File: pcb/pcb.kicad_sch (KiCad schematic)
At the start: 15 parts

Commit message: Shift to 2.2k resistors and 2V LEDs for brightness
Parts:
- R1, R2: LCSC C17539 -> C17533; MPN RSF100JB-73-6K8 -> MFR01SF2201A10
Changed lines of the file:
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@@
 			(effects (font (size 1.27 1.27)) hide)
 		)
-		(property "MPN" "RSF100JB-73-6K8" (at 114.3 50.8 0)
+		(property "MPN" "MFR01SF2201A10" (at 114.3 50.8 0)
 			(effects (font (size 1.27 1.27)) hide)
 		)
-		(property "LCSC" "C17539" (at 114.3 50.8 0)
+		(property "LCSC" "C17533" (at 114.3 50.8 0)
 			(effects (font (size 1.27 1.27)) hide)
 		)
@@
 			(effects (font (size 1.27 1.27)) hide)
 		)
-		(property "MPN" "RSF100JB-73-6K8" (at 114.3 88.9 0)
+		(property "MPN" "MFR01SF2201A10" (at 114.3 88.9 0)
 			(effects (font (size 1.27 1.27)) hide)
 		)
-		(property "LCSC" "C17539" (at 114.3 88.9 0)
+		(property "LCSC" "C17533" (at 114.3 88.9 0)
 			(effects (font (size 1.27 1.27)) hide)
 		)

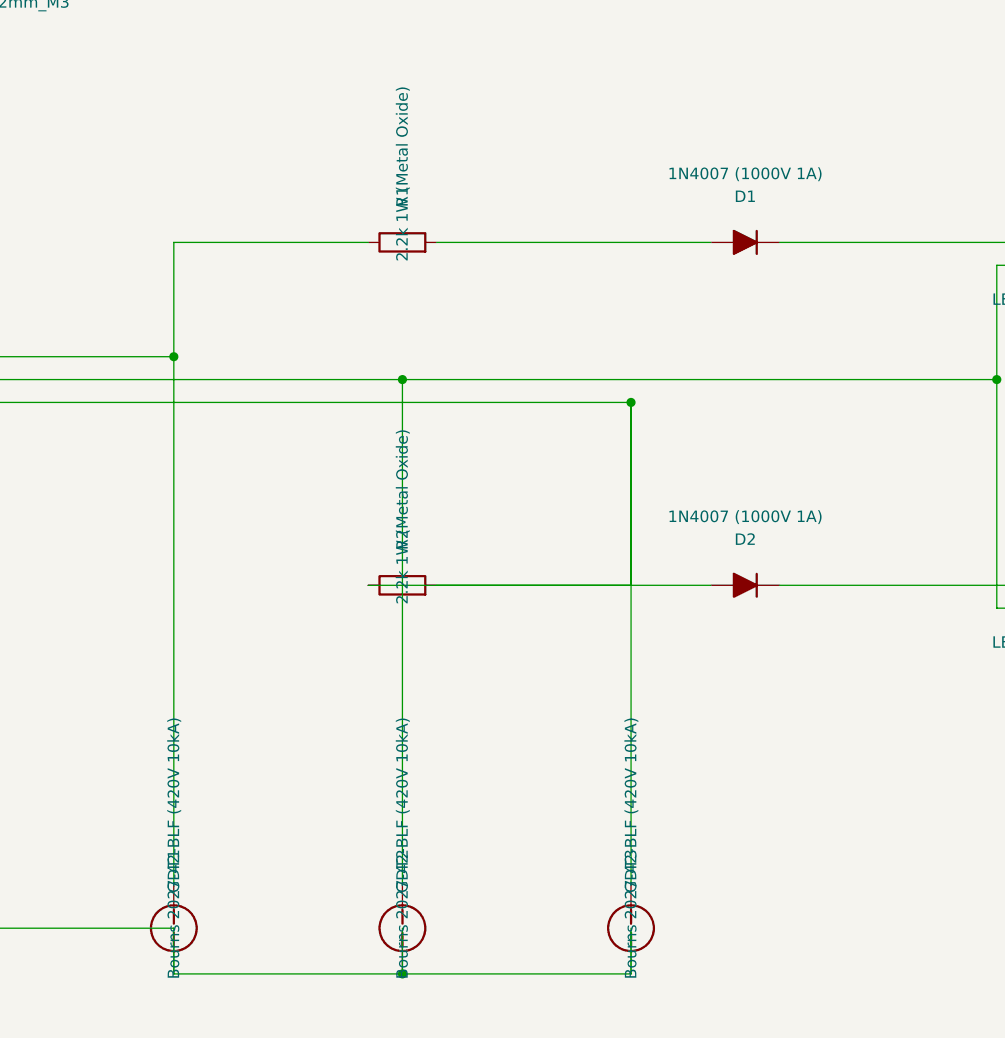
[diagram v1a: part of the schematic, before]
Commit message: Clean up pcb/ generated files in favour of Makefile and build/ dir
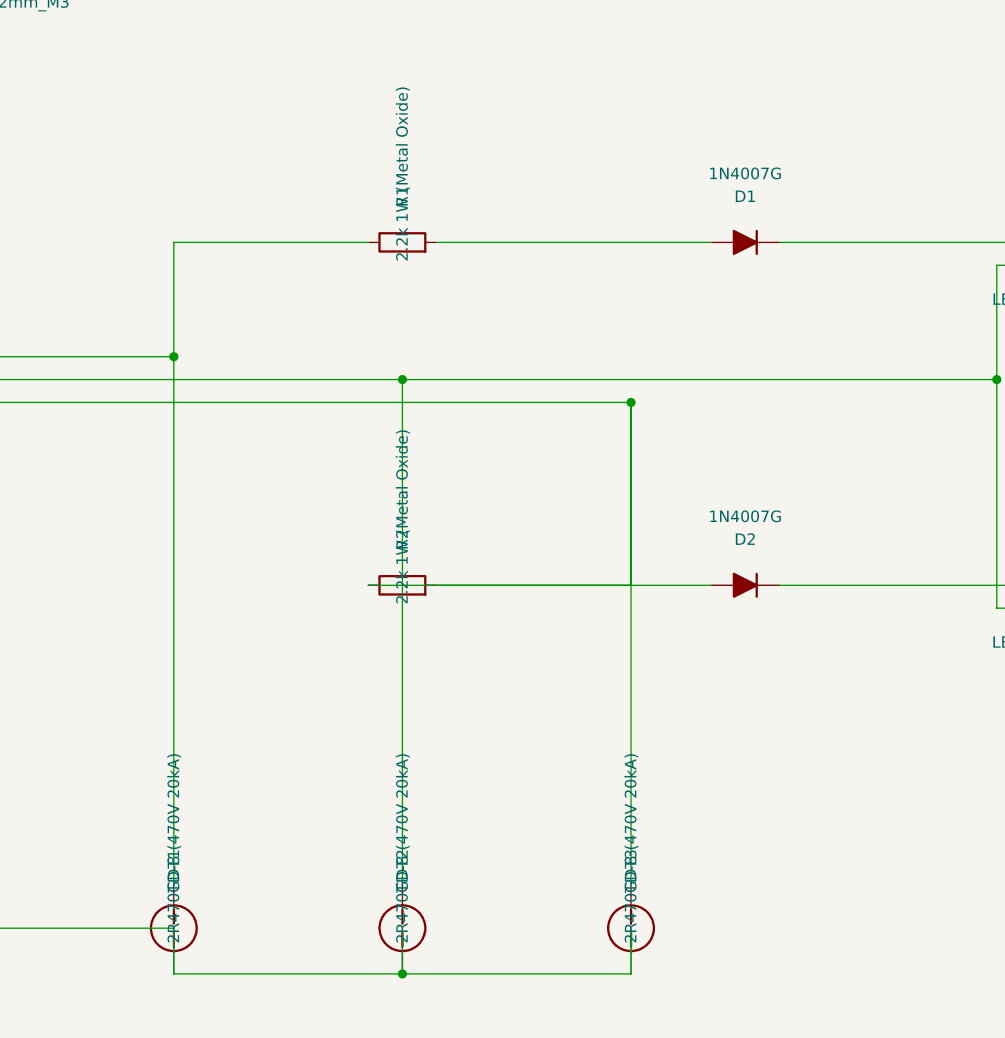
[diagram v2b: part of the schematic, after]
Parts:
- D1, D2: value 1N4007 (1000V 1A) -> 1N4007G; LCSC C2837 -> C232439; MPN 1N4007-E3/54 -> 1N4007G
- GDT1, GDT2, GDT3: value Bourns 2027-42-BLF (420V 10kA) -> 2R470TD-8 (470V 20kA); LCSC C2837330 -> C2836978; MPN 2027-42-BLF -> 2R470TD-8
- J_EARTH, J_LED_A, J_LED_C: LCSC C8464 -> C475092; MPN MKDS 1,5/ 2-5,08 -> KF129-5.08-2P
- J_IN: LCSC C8465 -> C474953; MPN MKDS 1,5/ 3-5,08 -> KF128-5.08-3P
- R1, R2: LCSC C17533 -> ASSIGN_BY_JLCPCB
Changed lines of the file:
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@@
 			(effects (font (size 1.27 1.27)) hide)
 		)
-		(property "MPN" "MKDS 1,5/ 3-5,08" (at 38.1 63.5 0)
-			(effects (font (size 1.27 1.27)) hide)
-		)
-		(property "LCSC" "C8465" (at 38.1 63.5 0)
+		(property "MPN" "KF128-5.08-3P" (at 38.1 63.5 0)
+			(effects (font (size 1.27 1.27)) hide)
+		)
+		(property "LCSC" "C474953" (at 38.1 63.5 0)
 			(effects (font (size 1.27 1.27)) hide)
 		)
@@
 			(effects (font (size 1.27 1.27)) hide)
 		)
-		(property "MPN" "MKDS 1,5/ 2-5,08" (at 38.1 127 0)
-			(effects (font (size 1.27 1.27)) hide)
-		)
-		(property "LCSC" "C8464" (at 38.1 127 0)
+		(property "MPN" "KF129-5.08-2P" (at 38.1 127 0)
+			(effects (font (size 1.27 1.27)) hide)
+		)
+		(property "LCSC" "C475092" (at 38.1 127 0)
 			(effects (font (size 1.27 1.27)) hide)
 		)
@@
 			(effects (font (size 1.27 1.27)) hide)
 		)
-		(property "MPN" "MKDS 1,5/ 2-5,08" (at 190.5 50.8 0)
-			(effects (font (size 1.27 1.27)) hide)
-		)
-		(property "LCSC" "C8464" (at 190.5 50.8 0)
+		(property "MPN" "KF129-5.08-2P" (at 190.5 50.8 0)
+			(effects (font (size 1.27 1.27)) hide)
+		)
+		(property "LCSC" "C475092" (at 190.5 50.8 0)
 			(effects (font (size 1.27 1.27)) hide)
 		)
@@
 			(effects (font (size 1.27 1.27)) hide)
 		)
-		(property "MPN" "MKDS 1,5/ 2-5,08" (at 190.5 88.9 0)
-			(effects (font (size 1.27 1.27)) hide)
-		)
-		(property "LCSC" "C8464" (at 190.5 88.9 0)
+		(property "MPN" "KF129-5.08-2P" (at 190.5 88.9 0)
+			(effects (font (size 1.27 1.27)) hide)
+		)
+		(property "LCSC" "C475092" (at 190.5 88.9 0)
 			(effects (font (size 1.27 1.27)) hide)
 		)
@@
 			(effects (font (size 1.27 1.27)) hide)
 		)
-		(property "LCSC" "C17533" (at 114.3 50.8 0)
+		(property "LCSC" "ASSIGN_BY_JLCPCB" (at 114.3 50.8 0)
 			(effects (font (size 1.27 1.27)) hide)
 		)
@@
 			(effects (font (size 1.27 1.27)))
 		)
-		(property "Value" "1N4007 (1000V 1A)" (at 152.4 43.18 0)
+		(property "Value" "1N4007G" (at 152.4 43.18 0)
 			(effects (font (size 1.27 1.27)))
 		)
@@
 			(effects (font (size 1.27 1.27)) hide)
 		)
-		(property "MPN" "1N4007-E3/54" (at 152.4 50.8 0)
-			(effects (font (size 1.27 1.27)) hide)
-		)
-		(property "LCSC" "C2837" (at 152.4 50.8 0)
+		(property "MPN" "1N4007G" (at 152.4 50.8 0)
+			(effects (font (size 1.27 1.27)) hide)
+		)
+		(property "LCSC" "C232439" (at 152.4 50.8 0)
 			(effects (font (size 1.27 1.27)) hide)
 		)
@@
 			(effects (font (size 1.27 1.27)) hide)
 		)
-		(property "LCSC" "C17533" (at 114.3 88.9 0)
+		(property "LCSC" "ASSIGN_BY_JLCPCB" (at 114.3 88.9 0)
 			(effects (font (size 1.27 1.27)) hide)
 		)
@@
 			(effects (font (size 1.27 1.27)))
 		)
-		(property "Value" "1N4007 (1000V 1A)" (at 152.4 81.28 0)
+		(property "Value" "1N4007G" (at 152.4 81.28 0)
 			(effects (font (size 1.27 1.27)))
 		)
@@
 			(effects (font (size 1.27 1.27)) hide)
 		)
-		(property "MPN" "1N4007-E3/54" (at 152.4 88.9 0)
-			(effects (font (size 1.27 1.27)) hide)
-		)
-		(property "LCSC" "C2837" (at 152.4 88.9 0)
+		(property "MPN" "1N4007G" (at 152.4 88.9 0)
+			(effects (font (size 1.27 1.27)) hide)
+		)
+		(property "LCSC" "C232439" (at 152.4 88.9 0)
 			(effects (font (size 1.27 1.27)) hide)
 		)
@@
 			(effects (font (size 1.27 1.27)))
 		)
-		(property "Value" "Bourns 2027-42-BLF (420V 10kA)" (at 88.9 118.11 0)
+		(property "Value" "2R470TD-8 (470V 20kA)" (at 88.9 118.11 0)
 			(effects (font (size 1.27 1.27)))
 		)
@@
 			(effects (font (size 1.27 1.27)) hide)
 		)
-		(property "MPN" "2027-42-BLF" (at 88.9 127 0)
-			(effects (font (size 1.27 1.27)) hide)
-		)
-		(property "LCSC" "C2837330" (at 88.9 127 0)
+		(property "MPN" "2R470TD-8" (at 88.9 127 0)
+			(effects (font (size 1.27 1.27)) hide)
+		)
+		(property "LCSC" "C2836978" (at 88.9 127 0)
 			(effects (font (size 1.27 1.27)) hide)
 		)
@@
 			(effects (font (size 1.27 1.27)))
 		)
-		(property "Value" "Bourns 2027-42-BLF (420V 10kA)" (at 114.3 118.11 0)
+		(property "Value" "2R470TD-8 (470V 20kA)" (at 114.3 118.11 0)
 			(effects (font (size 1.27 1.27)))
 		)
@@
 			(effects (font (size 1.27 1.27)) hide)
 		)
-		(property "MPN" "2027-42-BLF" (at 114.3 127 0)
-			(effects (font (size 1.27 1.27)) hide)
-		)
-		(property "LCSC" "C2837330" (at 114.3 127 0)
+		(property "MPN" "2R470TD-8" (at 114.3 127 0)
+			(effects (font (size 1.27 1.27)) hide)
+		)
+		(property "LCSC" "C2836978" (at 114.3 127 0)
 			(effects (font (size 1.27 1.27)) hide)
 		)
@@
 			(effects (font (size 1.27 1.27)))
 		)
-		(property "Value" "Bourns 2027-42-BLF (420V 10kA)" (at 139.7 118.11 0)
+		(property "Value" "2R470TD-8 (470V 20kA)" (at 139.7 118.11 0)
 			(effects (font (size 1.27 1.27)))
 		)
@@
 			(effects (font (size 1.27 1.27)) hide)
 		)
-		(property "MPN" "2027-42-BLF" (at 139.7 127 0)
-			(effects (font (size 1.27 1.27)) hide)
-		)
-		(property "LCSC" "C2837330" (at 139.7 127 0)
-			(effects (font (size 1.27 1.27)) hide)
-		)
+		(property "MPN" "2R470TD-8" (at 139.7 127 0)
+			(effects (font (size 1.27 1.27)) hide)
+		)
+		(property "LCSC" "C2836978" (at 139.7 127 0)
+			(effects (font (size 1.27 1.27)) hide)
+		)

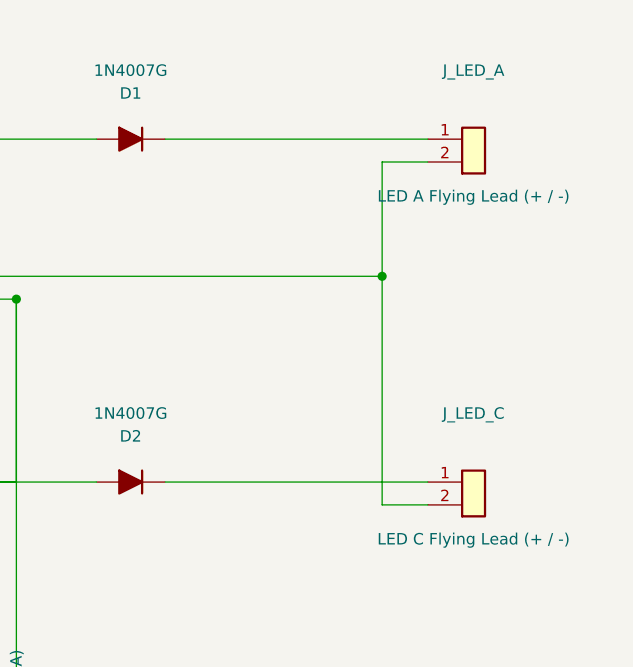
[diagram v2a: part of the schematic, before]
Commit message: v1.0.2 thanks to Kimi K3, cleanup LED_C pin semantics and docs
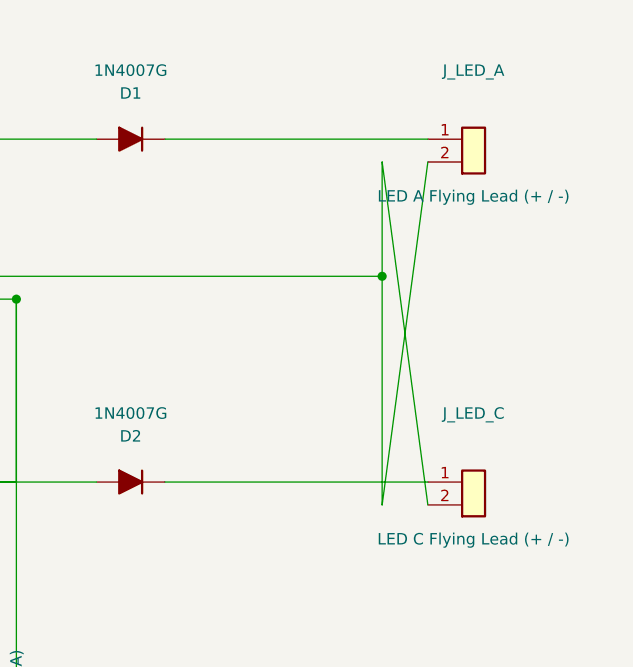
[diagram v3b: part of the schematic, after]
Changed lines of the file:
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@@
 		(title "Universal Milestone Indicator & Surge PCB")
 		(date "2026-08-22")
-		(rev "1.0")
+		(rev "1.0.2")
 		(company "DogFence Project")
 		(comment 1 "4km 3-Core DogWatch SmartFence Diagnostic & Surge System")
@@
 		(stroke (width 0) (type default))
 	)
-	(wire (pts (xy 180.34 53.34) (xy 185.42 53.34))
+	(wire (pts (xy 180.34 53.34) (xy 185.42 91.44))
 		(stroke (width 0) (type default))
 	)
@@
 	)
 	(junction (at 180.34 66.04) (diameter 1.016) (color 0 0 0 0))
-	(wire (pts (xy 180.34 91.44) (xy 185.42 91.44))
-		(stroke (width 0) (type default))
-	)
+	(wire (pts (xy 180.34 91.44) (xy 185.42 53.34))
+		(stroke (width 0) (type default))
+	)

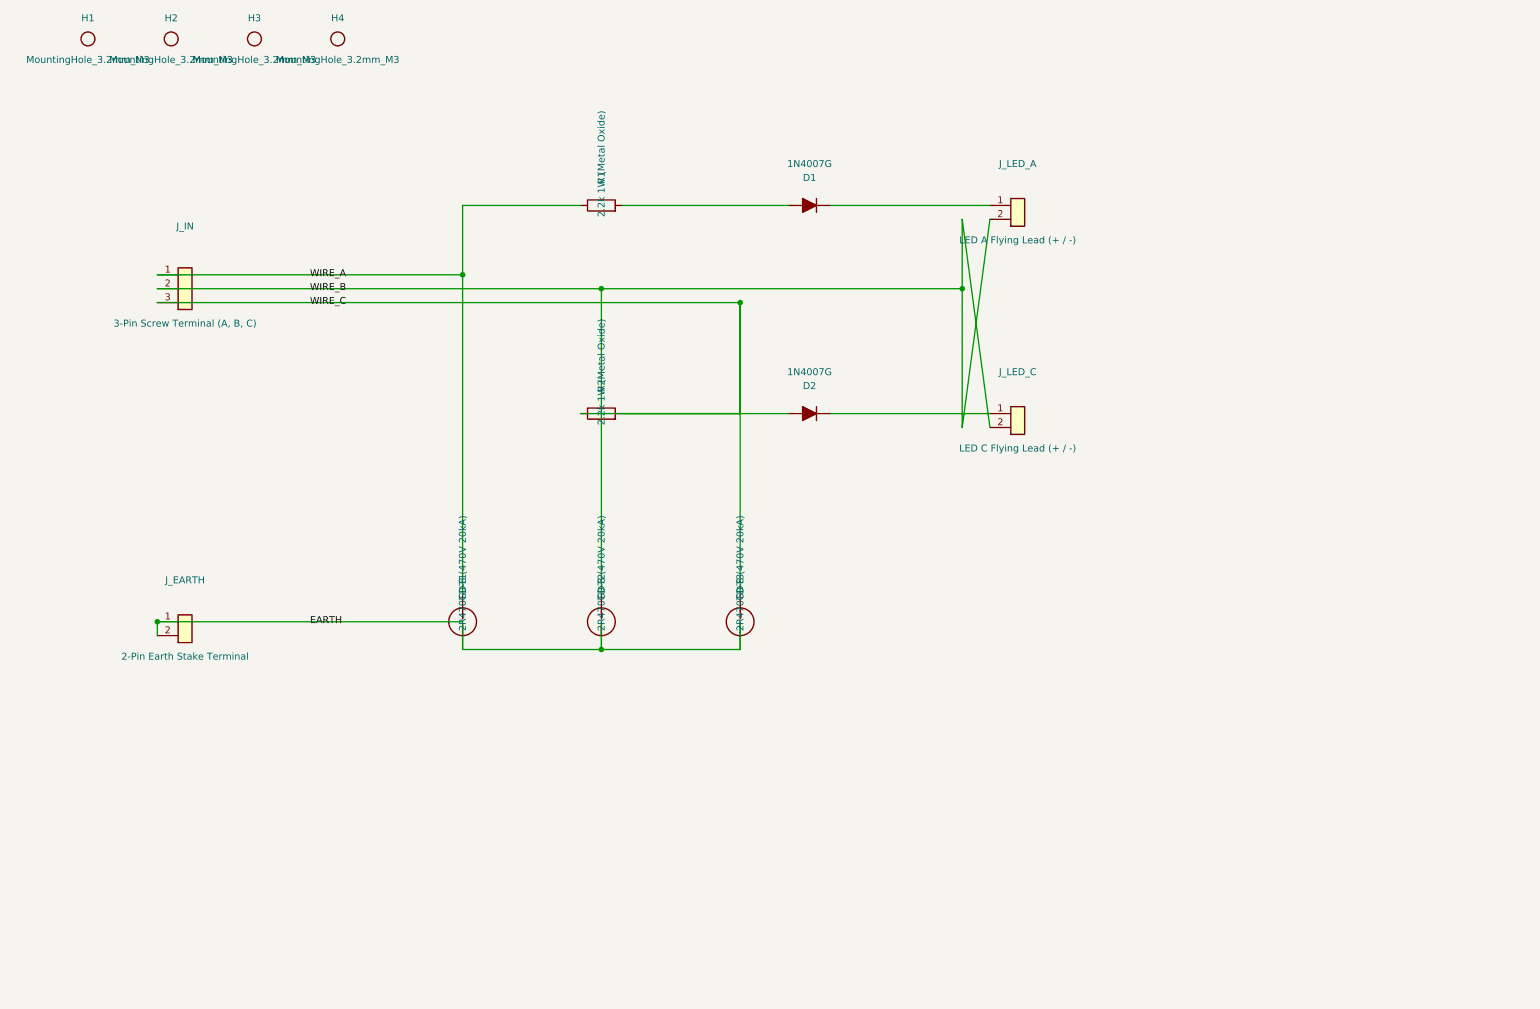
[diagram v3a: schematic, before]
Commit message: Gemini 3.8 Flash improvements to GDT locations and completeness
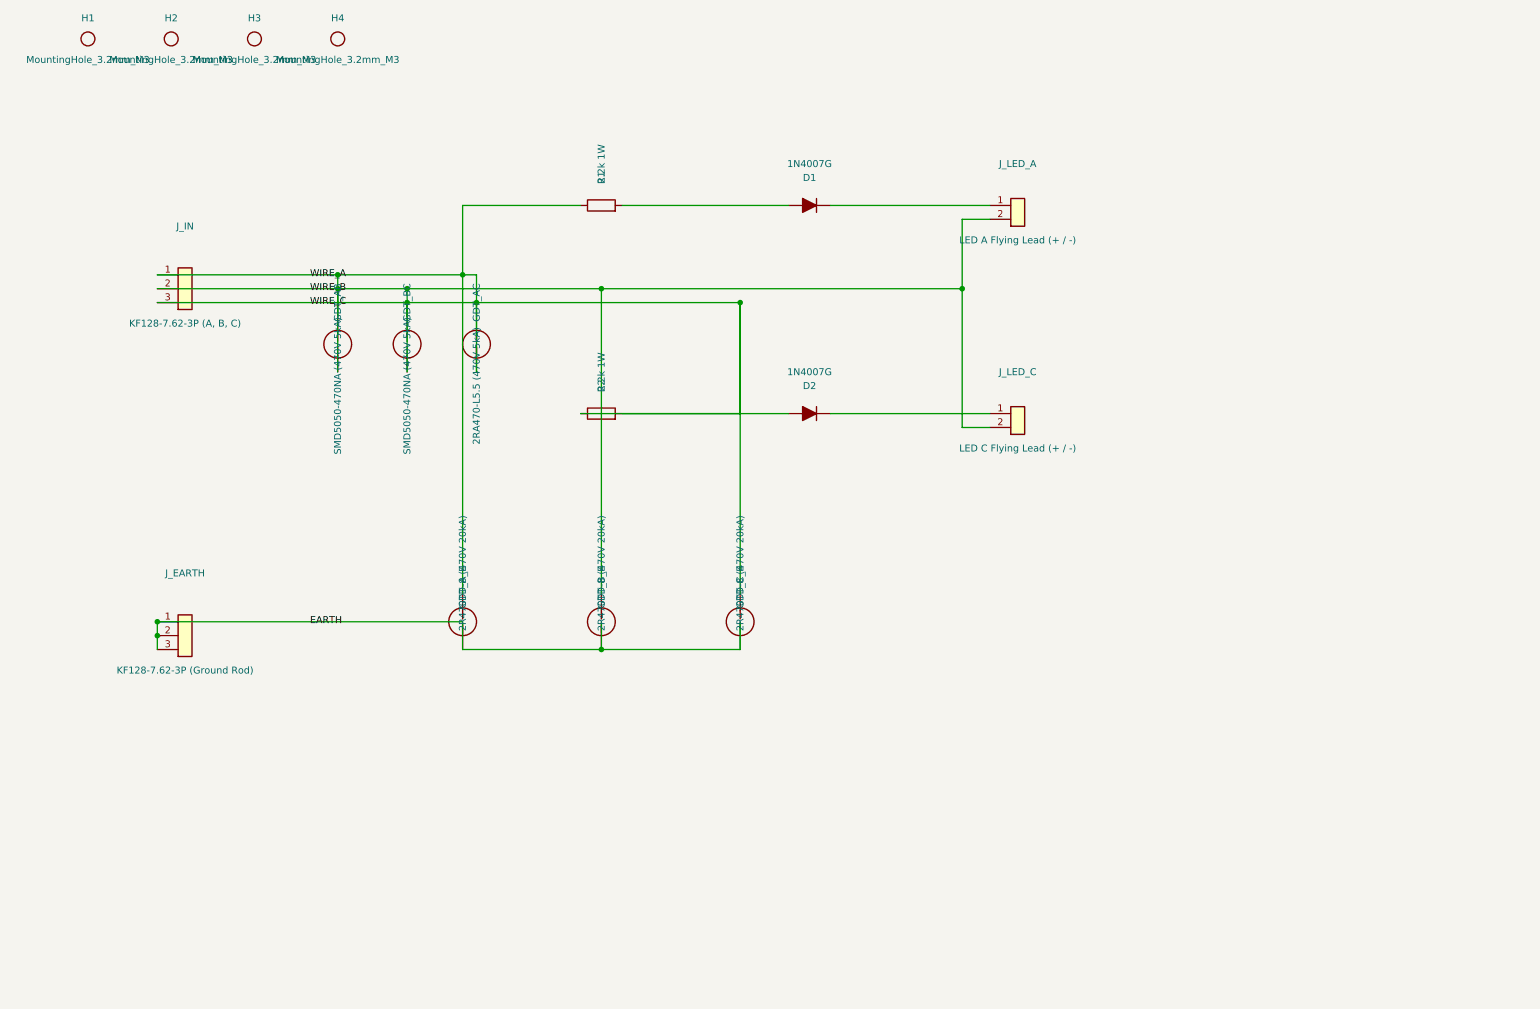
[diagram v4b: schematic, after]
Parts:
- added GDT_AB, GDT_BC: SMD5050-470NA (470V 5kA), GDT_SMD:GDT_SMD_5.0x5.0mm, symbol Device:GDT
- added GDT_AC: 2RA470-L5.5 (470V 5kA), Resistor_THT:R_Axial_DIN0617_L17.0mm_D6.0mm_P15.24mm_Horizontal, symbol Device:GDT
- GDT_A_E: renamed from GDT1; footprint Resistor_THT:R_Axial_DIN0617_L17.0mm_D6.0mm_P20.32mm_Horizontal -> Resistor_THT:R_Axial_DIN0617_L17.0mm_D6.0mm_P15.24mm_Horizontal; LCSC C2836978 -> C434855
- GDT_B_E: renamed from GDT2; footprint Resistor_THT:R_Axial_DIN0617_L17.0mm_D6.0mm_P20.32mm_Horizontal -> Resistor_THT:R_Axial_DIN0617_L17.0mm_D6.0mm_P15.24mm_Horizontal; LCSC C2836978 -> C434855
- GDT_C_E: renamed from GDT3; footprint Resistor_THT:R_Axial_DIN0617_L17.0mm_D6.0mm_P20.32mm_Horizontal -> Resistor_THT:R_Axial_DIN0617_L17.0mm_D6.0mm_P15.24mm_Horizontal; LCSC C2836978 -> C434855
- J_EARTH: value 2-Pin Earth Stake Terminal -> KF128-7.62-3P (Ground Rod); footprint TerminalBlock_Phoenix:TerminalBlock_Phoenix_MKDS-1,5-2-5.08_1x02_P5.08mm_Horizontal -> TerminalBlock_Phoenix:TerminalBlock_Phoenix_MKDS-1,5-3-7.62_1x03_P7.62mm_Horizontal; symbol Connector_Generic:Conn_01x02 -> Connector_Generic:Conn_01x03; LCSC C475092 -> ASSIGN_BY_JLCPCB; MPN KF129-5.08-2P -> KF128-7.62-3P
- J_IN: value 3-Pin Screw Terminal (A, B, C) -> KF128-7.62-3P (A, B, C); footprint TerminalBlock_Phoenix:TerminalBlock_Phoenix_MKDS-1,5-3-5.08_1x03_P5.08mm_Horizontal -> TerminalBlock_Phoenix:TerminalBlock_Phoenix_MKDS-1,5-3-7.62_1x03_P7.62mm_Horizontal; LCSC C474953 -> ASSIGN_BY_JLCPCB; MPN KF128-5.08-3P -> KF128-7.62-3P
- R1, R2: value 2.2k 1W (Metal Oxide) -> 2.2k 1W
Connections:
- net WIRE_B is gone; now on net WIRE_A: GDT_B_E.2, J_IN.2 (Pin_2), J_LED_A.2 (Pin_2), J_LED_C.2 (Pin_2)
- net WIRE_C is gone; now on net WIRE_A: D2.2 (A), GDT_C_E.2, J_IN.3 (Pin_3), R2.1, R2.2
- net EARTH: now also J_EARTH.3 (Pin_3)
- net WIRE_A: now also GDT_AB.1, GDT_AB.2, GDT_AC.1, GDT_AC.2, GDT_BC.1, GDT_BC.2
